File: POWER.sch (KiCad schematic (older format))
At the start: 58 parts

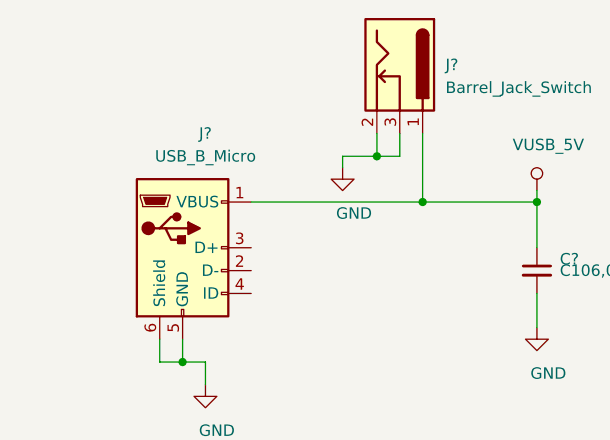
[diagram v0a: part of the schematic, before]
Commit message: add USB HOST,
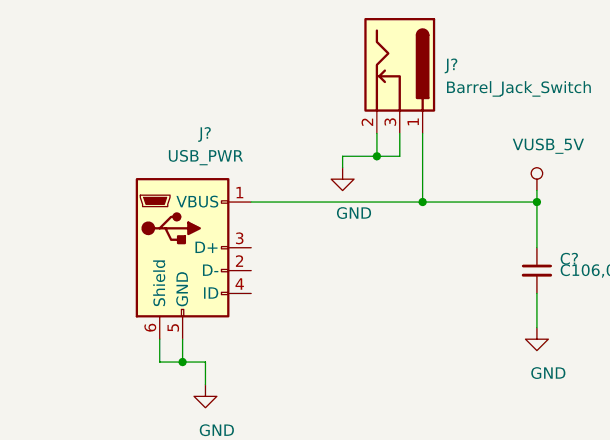
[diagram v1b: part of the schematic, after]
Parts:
- J?: value USB_B_Micro -> USB_PWR
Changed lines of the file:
@@
 P 4350 2250
 F 0 "J?" H 4450 2750 50  0000 C CNN
-F 1 "USB_B_Micro" H 4450 2650 50  0000 C CNN
+F 1 "USB_PWR" H 4450 2650 50  0000 C CNN
 F 2 "" H 4500 2200 50  0001 C CNN
 F 3 "~" H 4500 2200 50  0001 C CNN
